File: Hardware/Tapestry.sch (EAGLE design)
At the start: 81 parts, among them U1 ATSAMS70NXXA-AN, U2 AK4618VQ, U3 V_REG_MIC2920, U4 V_REG_MIC2920, U5 USD-SOCKETNEW, Y1 12MHZ

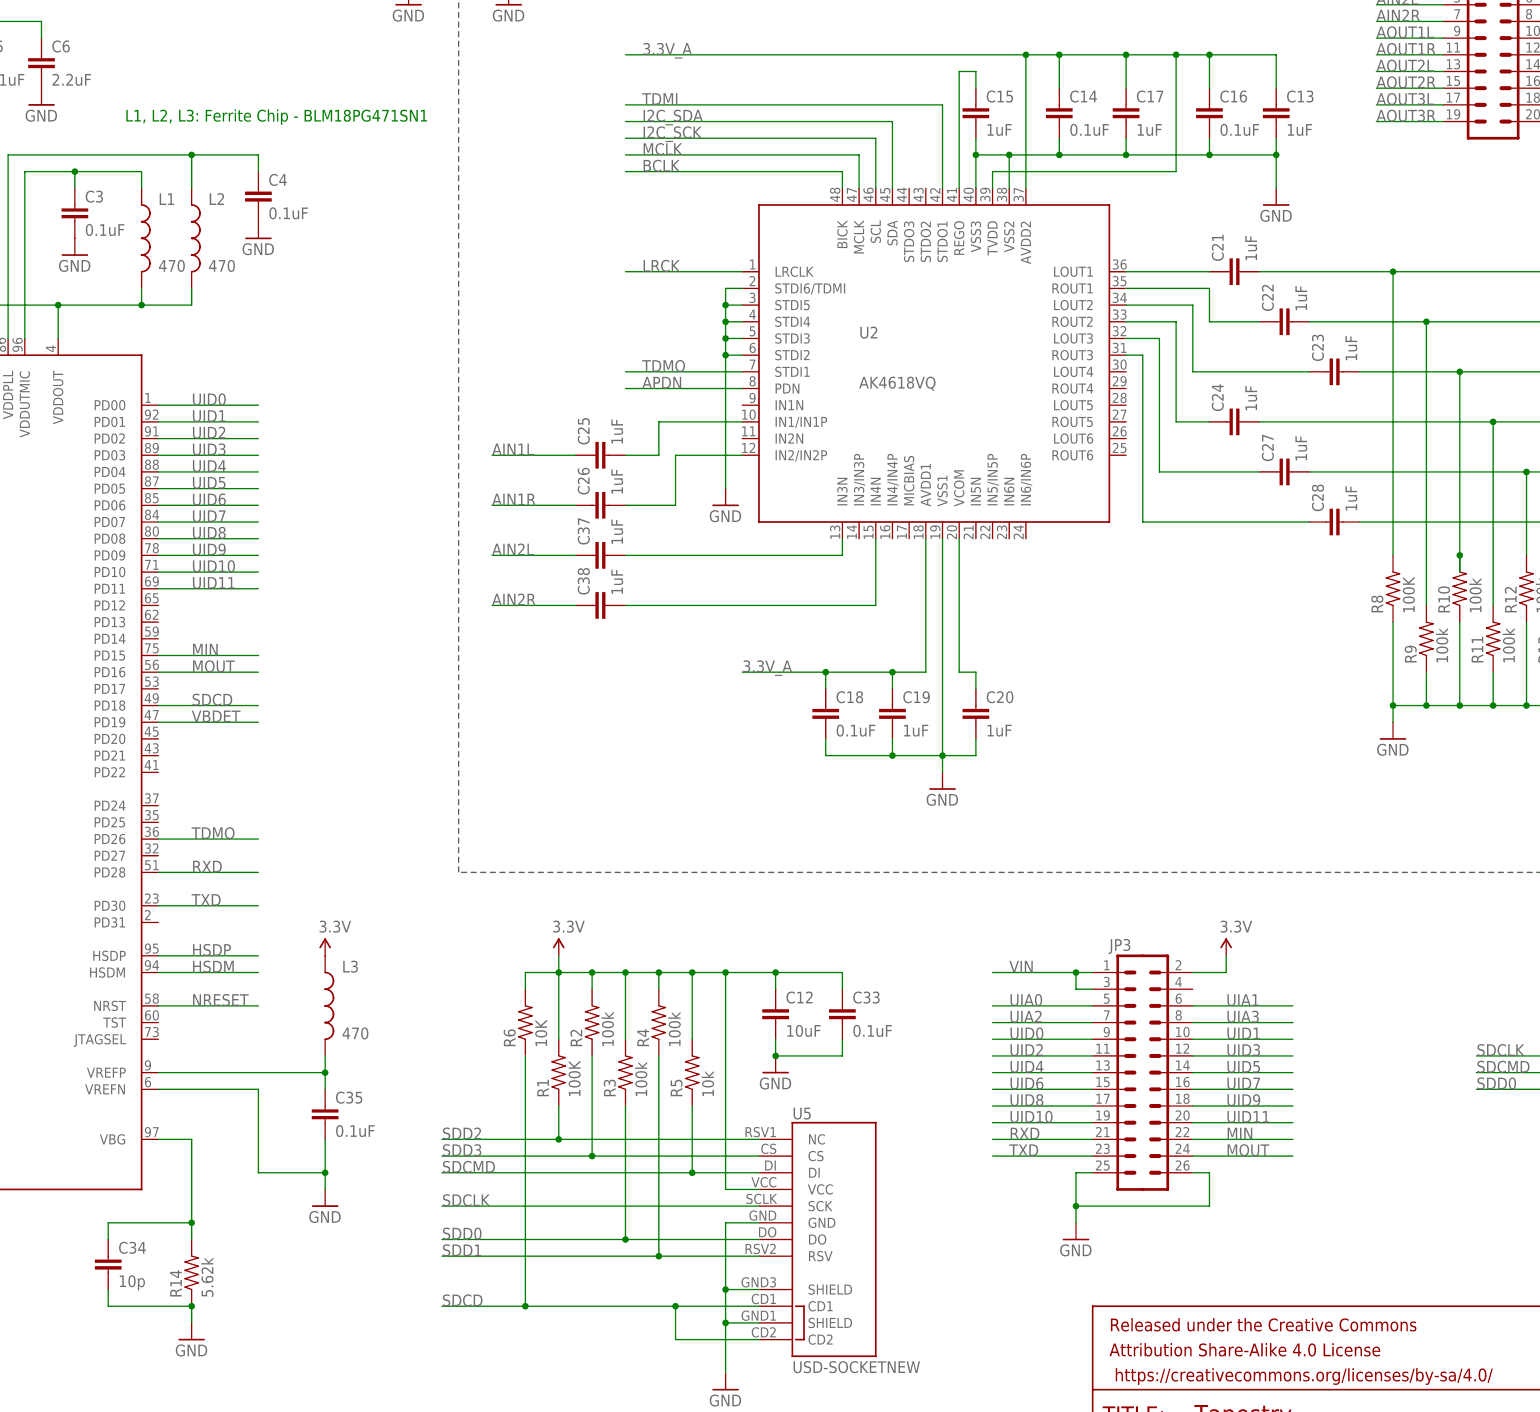
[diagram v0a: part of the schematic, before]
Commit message: Replaced generic resistors and capacitors with SparkFun versions.
Signed-off-by: robertsonics <jamie@robertsonics.com>
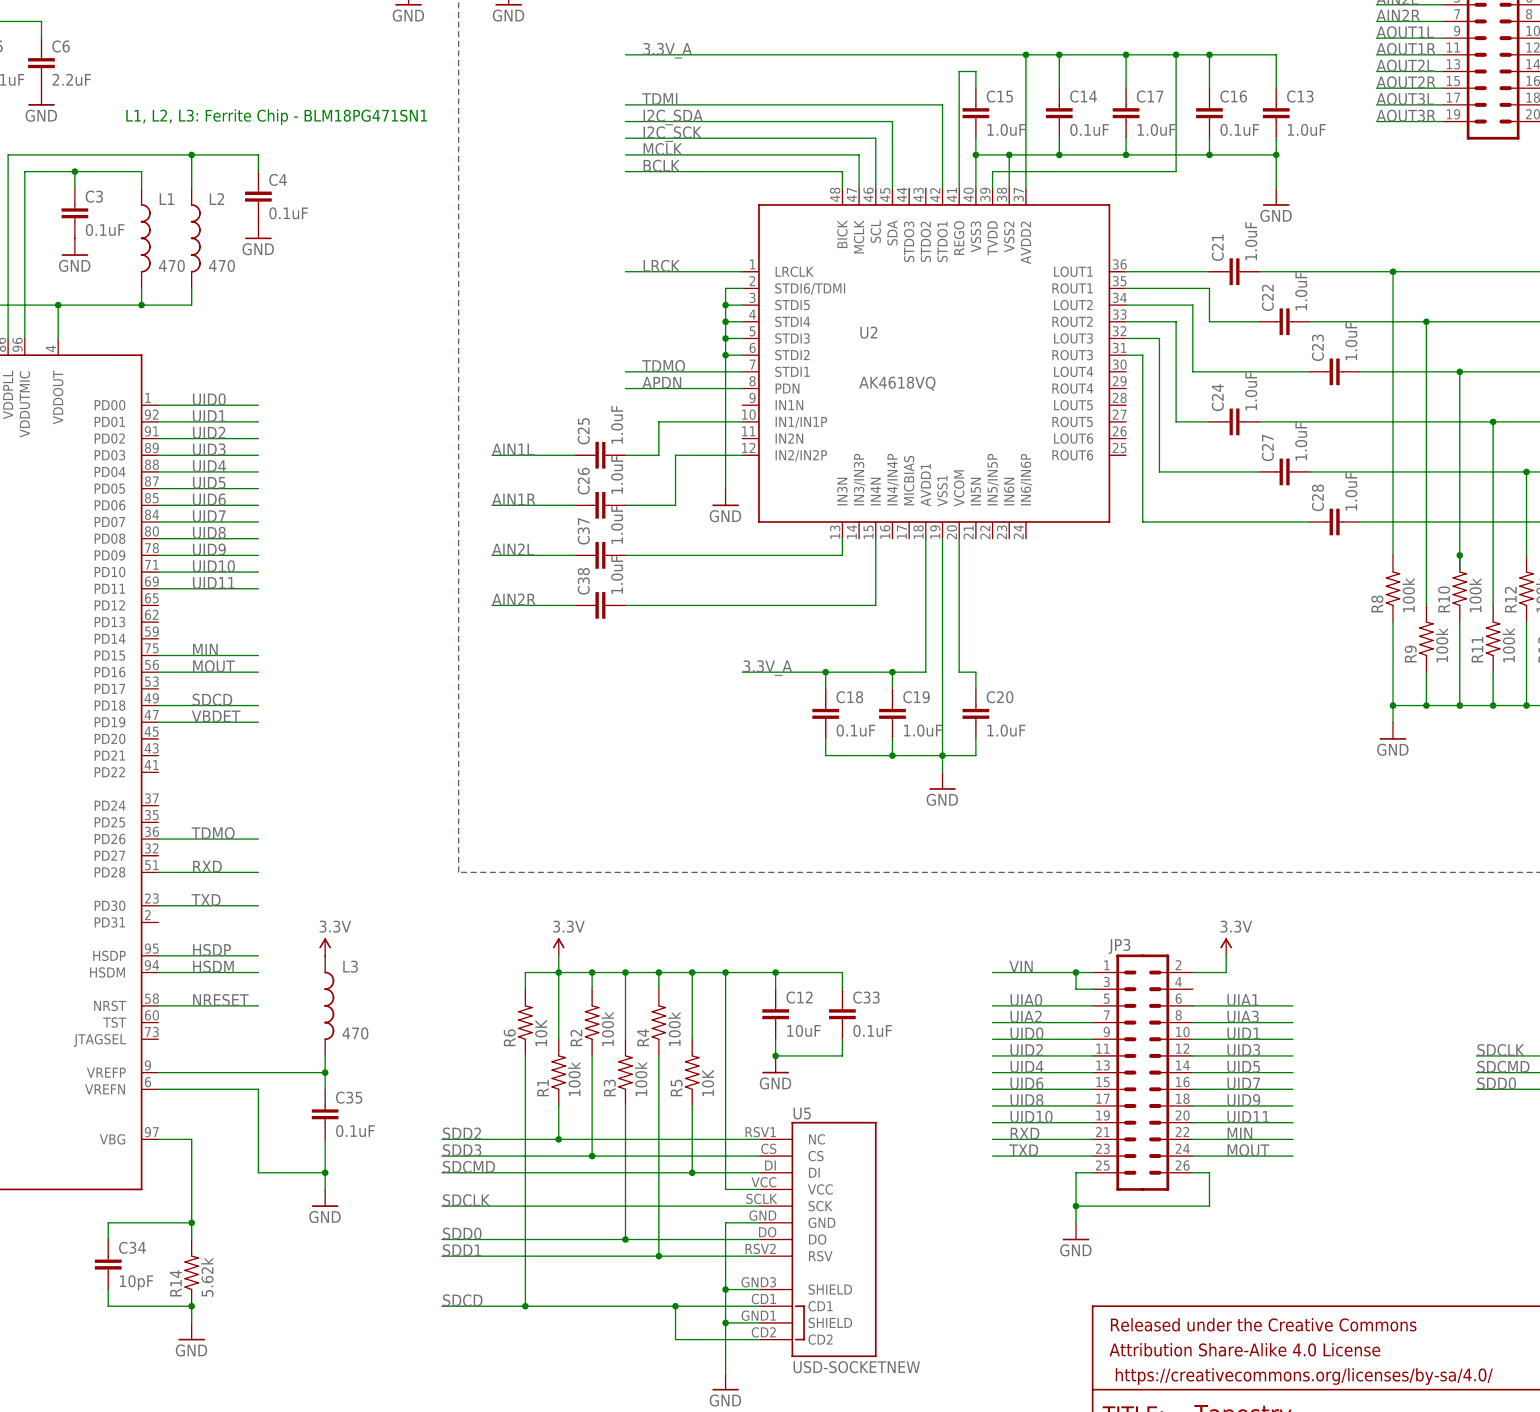
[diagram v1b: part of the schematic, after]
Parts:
- C1, C2: device SparkFun-Capacitors:CAP0603-CAP -> SparkFun-Capacitors:12PF-50V-5%(0603)
- C10, C14, C16, C18, C3, C33, C35, C4, C5, C8: device SparkFun-Capacitors:CAP0603-CAP -> SparkFun-Capacitors:0.1UF-25V(+80/-20%)(0603)
- C11, C12, C36, C9: device SparkFun-Capacitors:CAP0603-CAP -> SparkFun-Capacitors:10UF-6.3V-20%(0603)
- C13, C15, C17, C19, C20, C21, C22, C23, C24, C25, C26, C27, C28, C37, C38: value 1uF -> 1.0uF; device SparkFun-Capacitors:CAP0603-CAP -> SparkFun-Capacitors:1.0UF-16V-10%(0603)
- C34: value 10p -> 10pF; device SparkFun-Capacitors:CAP0603-CAP -> SparkFun-Capacitors:10PF-50V-5%(0603)
- C6: device SparkFun-Capacitors:CAP0603-CAP -> SparkFun-Capacitors:2.2UF-10V-20%(0603)
- R1, R8: value 100K -> 100k; device SparkFun-Resistors:RESISTOR0603-RES -> SparkFun-Resistors:100KOHM-1/10W-1%(0603)
- R10, R11, R12, R13, R2, R3, R4, R9: device SparkFun-Resistors:RESISTOR0603-RES -> SparkFun-Resistors:100KOHM-1/10W-1%(0603)
- R14: device SparkFun-Resistors:RESISTOR0603-RES -> SparkFun-Resistors:5.62KOHM1/10W1%(0603)
- R15: device SparkFun-Resistors:RESISTOR0603-RES -> SparkFun-Resistors:15KOHM1/10W1%(0603)0603
- R16: device SparkFun-Resistors:RESISTOR0603-RES -> SparkFun-Resistors:22KOHM1/10W1%(0603)
- R5: value 10k -> 10K; device SparkFun-Resistors:RESISTOR0603-RES -> SparkFun-Resistors:10KOHM-1/10W-1%(0603)0603
- R6: device SparkFun-Resistors:RESISTOR0603-RES -> SparkFun-Resistors:10KOHM-1/10W-1%(0603)0603
- R7: device SparkFun-Resistors:RESISTOR0603-RES -> SparkFun-Resistors:330OHM1/10W1%(0603)

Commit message: First pass over schematic.
Mostly changing flag style on signals.
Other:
- moved on the sheet: C25, C26, C37, C38

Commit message: Second pass over schematic
-Swapped crystal for smaller one.
-Updated SD card connector with SDIO signal names.
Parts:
- removed U5: USD-SOCKETNEW, SparkFun-Connectors:USD-SOCKETNEW
- added JP5: USD-SDIO-SOCKET, SparkFun-Connectors:USD-SDIO-SOCKET
- Y1: value 12MHZ -> 12MHz; device SparkFun-FreqCtrl:CRYSTALSMD -> SparkFun-FreqCtrl:CRYSTALCRYSTAL-SMD-5X3-12MHZ
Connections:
- net 3.3V: now also JP5.VCC; no longer U5.VCC
- net GND: now also JP5.GND, JP5.SHIELD@1, JP5.SHIELD@3; no longer U5.GND, U5.SHIELD@1, U5.SHIELD@3
- net SDCD: now also JP5.CD1, JP5.CD2; no longer U5.CD1, U5.CD2
- net SDCLK: now also JP5.CLK; no longer U5.SCK
- net SDCMD: now also JP5.CMD; no longer U5.DI
- net SDD0: now also JP5.DAT0; no longer U5.DO
- net SDD1: now also JP5.DAT1; no longer U5.RSV
- net SDD2: now also JP5.DAT2; no longer U5.NC
- net SDD3: now also JP5.CD/DAT3; no longer U5.CS
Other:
- note added: "Jamie Robertson & Byron Jacquot"
- note added: "V01"
- moved on the sheet: C15
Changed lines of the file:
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@@
 <part name="U1" library="tapestry" deviceset="ATSAMS70NXXA-AN" device=""/>
 <part name="FRAME1" library="SparkFun-Aesthetics" deviceset="FRAME-LEDGER" device=""/>
-<part name="U5" library="SparkFun-Connectors" deviceset="USD-SOCKET" device="NEW"/>
 <part name="JP1" library="SparkFun-Connectors" deviceset="USB" device="SMD"/>
-<part name="Y1" library="SparkFun-FreqCtrl" deviceset="CRYSTAL" device="SMD" value="12MHZ"/>
+<part name="Y1" library="SparkFun-FreqCtrl" deviceset="CRYSTAL" device="CRYSTAL-SMD-5X3-12MHZ" value="12MHz"/>
 <part name="C1" library="SparkFun-Capacitors" deviceset="12PF-50V-5%(0603)" device="" value="12pF"/>
 <part name="C2" library="SparkFun-Capacitors" deviceset="12PF-50V-5%(0603)" device="" value="12pF"/>
@@
 <part name="C32" library="SparkFun-Capacitors" deviceset="0.1UF-100V-10%(0603)" device="" value="0.1uF"/>
 <part name="D1" library="SparkFun-LED" deviceset="LED-BLUE" device="0603" value="BLUE"/>
+<part name="JP5" library="SparkFun-Connectors" deviceset="USD-SDIO-SOCKET" device=""/>
 </parts>
 <sheets>
@@
 <wire x1="419.1" y1="101.6" x2="233.68" y2="101.6" width="0.1524" layer="97" style="shortdash"/>
 <wire x1="233.68" y1="101.6" x2="233.68" y2="261.62" width="0.1524" layer="97" style="shortdash"/>
+<text x="335.28" y="7.62" size="2.54" layer="94" font="vector">Jamie Robertson &amp; Byron Jacquot</text>
+<text x="421.64" y="7.62" size="2.54" layer="94" font="vector">V01</text>
 </plain>
 <instances>
@@
 <instance part="FRAME1" gate="G$1" x="0" y="0"/>
 <instance part="FRAME1" gate="G$2" x="330.2" y="0"/>
-<instance part="U5" gate="G$1" x="287.02" y="48.26"/>
 <instance part="JP1" gate="G$1" x="38.1" y="177.8" rot="MR0"/>
 <instance part="Y1" gate="G$1" x="73.66" y="66.04" rot="R180"/>
@@
 <instance part="C13" gate="G$1" x="358.14" y="215.9"/>
 <instance part="C14" gate="G$1" x="325.12" y="215.9"/>
-<instance part="C15" gate="G$1" x="312.42" y="215.9"/>
+<instance part="C15" gate="G$1" x="314.96" y="215.9"/>
 <instance part="C16" gate="G$1" x="347.98" y="215.9"/>
 <instance part="C17" gate="G$1" x="335.28" y="215.9"/>
@@
 <instance part="C32" gate="G$1" x="63.5" y="27.94"/>
 <instance part="D1" gate="G$1" x="66.04" y="121.92"/>
+<instance part="JP5" gate="G$1" x="287.02" y="27.94"/>
 </instances>
 <busses>
@@
 </segment>
 <segment>
-<pinref part="U5" gate="G$1" pin="GND"/>
 <pinref part="GND12" gate="1" pin="GND"/>
-<wire x1="279.4" y1="48.26" x2="274.32" y2="48.26" width="0.1524" layer="91"/>
+<wire x1="281.94" y1="48.26" x2="274.32" y2="48.26" width="0.1524" layer="91"/>
 <wire x1="274.32" y1="48.26" x2="274.32" y2="38.1" width="0.1524" layer="91"/>
-<pinref part="U5" gate="G$1" pin="SHIELD@1"/>
 <wire x1="274.32" y1="38.1" x2="274.32" y2="33.02" width="0.1524" layer="91"/>
 <wire x1="274.32" y1="33.02" x2="274.32" y2="25.4" width="0.1524" layer="91"/>
-<wire x1="279.4" y1="38.1" x2="274.32" y2="38.1" width="0.1524" layer="91"/>
-<pinref part="U5" gate="G$1" pin="SHIELD@3"/>
-<wire x1="279.4" y1="33.02" x2="274.32" y2="33.02" width="0.1524" layer="91"/>
+<wire x1="281.94" y1="38.1" x2="274.32" y2="38.1" width="0.1524" layer="91"/>
+<wire x1="281.94" y1="33.02" x2="274.32" y2="33.02" width="0.1524" layer="91"/>
 <junction x="274.32" y="38.1"/>
 <junction x="274.32" y="33.02"/>
+<pinref part="JP5" gate="G$1" pin="GND"/>
+<pinref part="JP5" gate="G$1" pin="SHIELD@3"/>
+<pinref part="JP5" gate="G$1" pin="SHIELD@1"/>
 </segment>
 <segment>
@@
 <pinref part="U2" gate="G$1" pin="VSS3"/>
 <wire x1="312.42" y1="205.74" x2="312.42" y2="210.82" width="0.1524" layer="91"/>
-<wire x1="312.42" y1="210.82" x2="317.5" y2="210.82" width="0.1524" layer="91"/>
+<wire x1="312.42" y1="210.82" x2="314.96" y2="210.82" width="0.1524" layer="91"/>
+<wire x1="314.96" y1="210.82" x2="317.5" y2="210.82" width="0.1524" layer="91"/>
 <wire x1="317.5" y1="210.82" x2="325.12" y2="210.82" width="0.1524" layer="91"/>
 <wire x1="325.12" y1="210.82" x2="335.28" y2="210.82" width="0.1524" layer="91"/>
@@
 <junction x="325.12" y="210.82"/>
 <pinref part="C15" gate="G$1" pin="2"/>
-<wire x1="312.42" y1="213.36" x2="312.42" y2="210.82" width="0.1524" layer="91"/>
+<wire x1="314.96" y1="213.36" x2="314.96" y2="210.82" width="0.1524" layer="91"/>
+<wire x1="314.96" y1="210.82" x2="312.42" y2="210.82" width="0.1524" layer="91"/>
 <junction x="312.42" y="210.82"/>
 <pinref part="C16" gate="G$1" pin="2"/>
@@
 <wire x1="335.28" y1="213.36" x2="335.28" y2="210.82" width="0.1524" layer="91"/>
 <junction x="335.28" y="210.82"/>
+<junction x="314.96" y="210.82"/>
 </segment>
 <segment>
@@
 <wire x1="269.24" y1="86.36" x2="274.32" y2="86.36" width="0.1524" layer="91"/>
 <wire x1="274.32" y1="86.36" x2="274.32" y2="53.34" width="0.1524" layer="91"/>
-<pinref part="U5" gate="G$1" pin="VCC"/>
-<wire x1="274.32" y1="53.34" x2="279.4" y2="53.34" width="0.1524" layer="91"/>
+<wire x1="274.32" y1="53.34" x2="281.94" y2="53.34" width="0.1524" layer="91"/>
 <pinref part="C12" gate="G$1" pin="1"/>
 <wire x1="274.32" y1="86.36" x2="281.94" y2="86.36" width="0.1524" layer="91"/>
@@
 <wire x1="292.1" y1="86.36" x2="292.1" y2="83.82" width="0.1524" layer="91"/>
 <junction x="281.94" y="86.36"/>
+<pinref part="JP5" gate="G$1" pin="VCC"/>
 </segment>
 <segment>
@@
 </segment>
 <segment>
-<pinref part="U5" gate="G$1" pin="DO"/>
-<wire x1="279.4" y1="45.72" x2="259.08" y2="45.72" width="0.1524" layer="91"/>
+<wire x1="281.94" y1="45.72" x2="259.08" y2="45.72" width="0.1524" layer="91"/>
 <label x="238.76" y="45.72" size="1.27" layer="95" rot="R180" xref="yes"/>
 <pinref part="R3" gate="G$1" pin="1"/>
@@
 <wire x1="259.08" y1="66.04" x2="259.08" y2="45.72" width="0.1524" layer="91"/>
 <junction x="259.08" y="45.72"/>
+<pinref part="JP5" gate="G$1" pin="DAT0"/>
 </segment>
 <segment>
@@
 </segment>
 <segment>
-<pinref part="U5" gate="G$1" pin="RSV"/>
-<wire x1="279.4" y1="43.18" x2="264.16" y2="43.18" width="0.1524" layer="91"/>
+<wire x1="281.94" y1="43.18" x2="264.16" y2="43.18" width="0.1524" layer="91"/>
 <label x="238.76" y="43.18" size="1.27" layer="95" rot="R180" xref="yes"/>
 <pinref part="R4" gate="G$1" pin="1"/>
@@
 <wire x1="264.16" y1="73.66" x2="264.16" y2="43.18" width="0.1524" layer="91"/>
 <junction x="264.16" y="43.18"/>
+<pinref part="JP5" gate="G$1" pin="DAT1"/>
 </segment>
 </net>
@@
 </segment>
 <segment>
-<pinref part="U5" gate="G$1" pin="NC"/>
-<wire x1="279.4" y1="60.96" x2="248.92" y2="60.96" width="0.1524" layer="91"/>
+<wire x1="281.94" y1="60.96" x2="248.92" y2="60.96" width="0.1524" layer="91"/>
 <label x="238.76" y="60.96" size="1.27" layer="95" rot="R180" xref="yes"/>
 <pinref part="R1" gate="G$1" pin="1"/>
@@
 <wire x1="248.92" y1="66.04" x2="248.92" y2="60.96" width="0.1524" layer="91"/>
 <junction x="248.92" y="60.96"/>
+<pinref part="JP5" gate="G$1" pin="DAT2"/>
 </segment>
 </net>
@@
 </segment>
 <segment>
-<pinref part="U5" gate="G$1" pin="CS"/>
-<wire x1="279.4" y1="58.42" x2="254" y2="58.42" width="0.1524" layer="91"/>
+<wire x1="281.94" y1="58.42" x2="254" y2="58.42" width="0.1524" layer="91"/>
 <label x="238.76" y="58.42" size="1.27" layer="95" rot="R180" xref="yes"/>
 <pinref part="R2" gate="G$1" pin="1"/>
@@
 <wire x1="254" y1="73.66" x2="254" y2="58.42" width="0.1524" layer="91"/>
 <junction x="254" y="58.42"/>
+<pinref part="JP5" gate="G$1" pin="CD/DAT3"/>
 </segment>
 </net>
@@
 </segment>
 <segment>
-<pinref part="U5" gate="G$1" pin="SCK"/>
-<wire x1="279.4" y1="50.8" x2="238.76" y2="50.8" width="0.1524" layer="91"/>
+<wire x1="281.94" y1="50.8" x2="238.76" y2="50.8" width="0.1524" layer="91"/>
 <label x="238.76" y="50.8" size="1.27" layer="95" rot="R180" xref="yes"/>
+<pinref part="JP5" gate="G$1" pin="CLK"/>
 </segment>
 <segment>
@@
 </segment>
 <segment>
-<pinref part="U5" gate="G$1" pin="DI"/>
-<wire x1="279.4" y1="55.88" x2="269.24" y2="55.88" width="0.1524" layer="91"/>
+<wire x1="281.94" y1="55.88" x2="269.24" y2="55.88" width="0.1524" layer="91"/>
 <label x="238.76" y="55.88" size="1.27" layer="95" rot="R180" xref="yes"/>
 <pinref part="R5" gate="G$1" pin="1"/>
@@
 <wire x1="269.24" y1="66.04" x2="269.24" y2="55.88" width="0.1524" layer="91"/>
 <junction x="269.24" y="55.88"/>
+<pinref part="JP5" gate="G$1" pin="CMD"/>
 </segment>
 <segment>
@@
 </segment>
 <segment>
-<pinref part="U5" gate="G$1" pin="CD1"/>
-<wire x1="279.4" y1="35.56" x2="266.7" y2="35.56" width="0.1524" layer="91"/>
-<pinref part="U5" gate="G$1" pin="CD2"/>
+<wire x1="281.94" y1="35.56" x2="266.7" y2="35.56" width="0.1524" layer="91"/>
 <wire x1="266.7" y1="35.56" x2="243.84" y2="35.56" width="0.1524" layer="91"/>
 <wire x1="243.84" y1="35.56" x2="238.76" y2="35.56" width="0.1524" layer="91"/>
-<wire x1="279.4" y1="30.48" x2="266.7" y2="30.48" width="0.1524" layer="91"/>
+<wire x1="281.94" y1="30.48" x2="266.7" y2="30.48" width="0.1524" layer="91"/>
 <wire x1="266.7" y1="30.48" x2="266.7" y2="35.56" width="0.1524" layer="91"/>
 <junction x="266.7" y="35.56"/>
@@
 <wire x1="243.84" y1="73.66" x2="243.84" y2="35.56" width="0.1524" layer="91"/>
 <junction x="243.84" y="35.56"/>
+<pinref part="JP5" gate="G$1" pin="CD1"/>
+<pinref part="JP5" gate="G$1" pin="CD2"/>
 </segment>
 </net>
@@
 <pinref part="U2" gate="G$1" pin="REGO"/>
 <wire x1="309.88" y1="205.74" x2="309.88" y2="223.52" width="0.1524" layer="91"/>
-<wire x1="309.88" y1="223.52" x2="312.42" y2="223.52" width="0.1524" layer="91"/>
+<wire x1="309.88" y1="223.52" x2="314.96" y2="223.52" width="0.1524" layer="91"/>
 <pinref part="C15" gate="G$1" pin="1"/>
-<wire x1="312.42" y1="223.52" x2="312.42" y2="220.98" width="0.1524" layer="91"/>
-</segment>
-</net>
+<wire x1="314.96" y1="223.52" x2="314.96" y2="220.98" width="0.1524" layer="91"/>
+</segment>
+</net>
